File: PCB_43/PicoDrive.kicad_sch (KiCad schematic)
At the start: 28 parts, among them J1 Conn_02x08_Row_Letter_Last, J3 OLED SCREEN CONN, J4 Micro_SD_Card_Det1, Q3 2N2219, U1 Pico, U2 TSR_1-2450

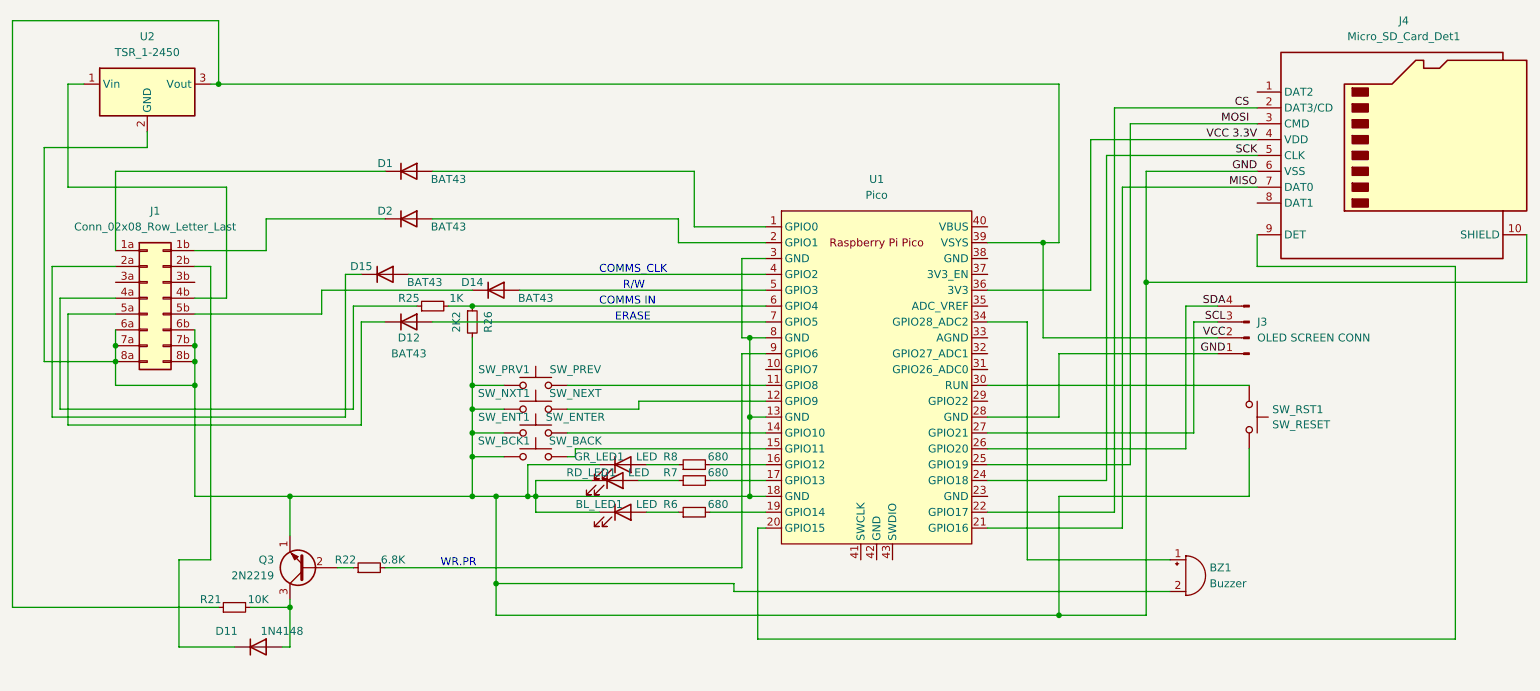
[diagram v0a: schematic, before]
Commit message: Added to PCB a connector for MDV_Control boards
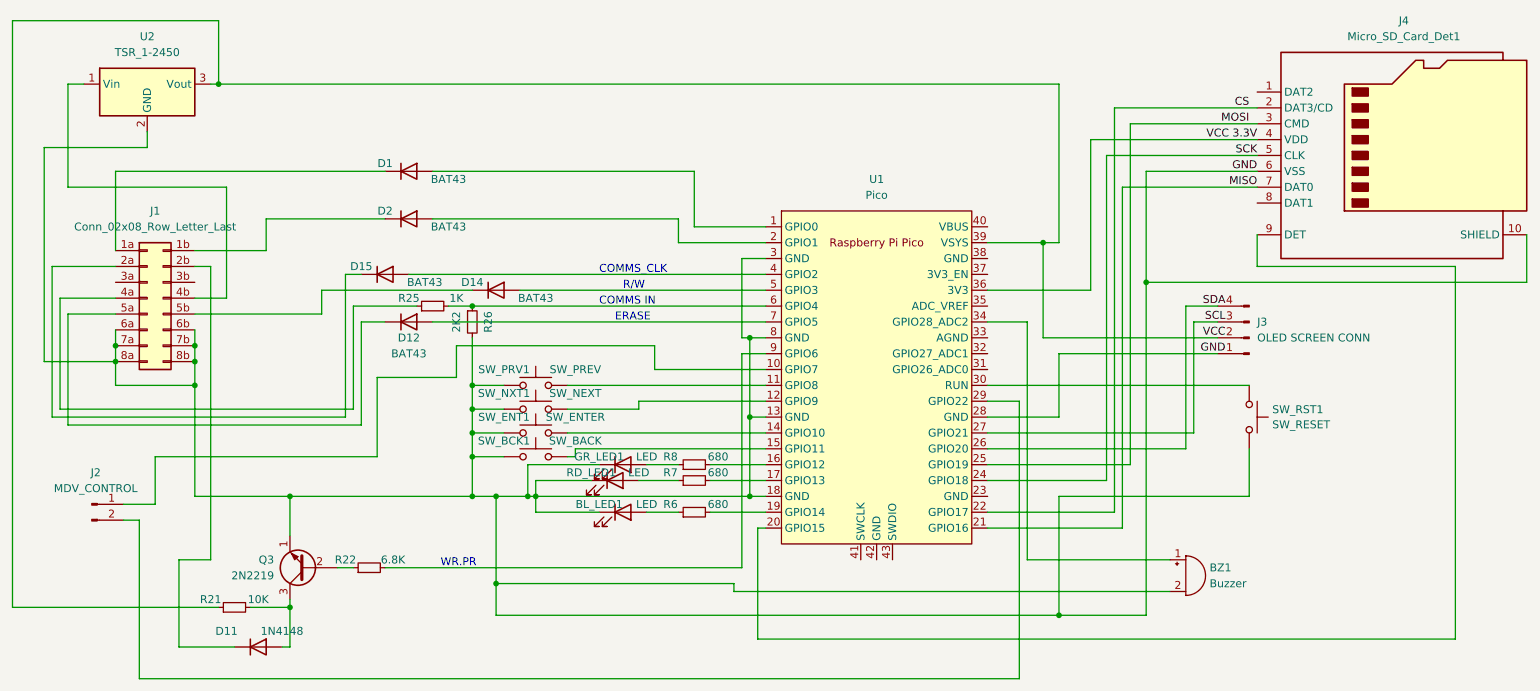
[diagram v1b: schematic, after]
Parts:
- added J2: MDV_CONTROL, Connector_PinHeader_2.54mm:PinHeader_1x02_P2.54mm_Vertical, symbol Connector:Conn_01x02_Pin
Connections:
- net at U1.10 (GPIO7): now also J2.1 (Pin_1)
- net at U1.29 (GPIO22): now also J2.2 (Pin_2)
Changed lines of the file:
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@@
+    (stroke (width 0) (type default))
+  )
+  (wire (pts (xy 88.9 91.44) (xy 53.34 91.44))
     (stroke (width 0) (type default))
   )
@@
     (stroke (width 0) (type default))
   )
+  (wire (pts (xy 53.34 91.44) (xy 53.34 99.06))
+    (stroke (width 0) (type default))
+  )
   (wire (pts (xy 146.05 113.03) (xy 215.9 113.03))
     (stroke (width 0) (type default))
@@
     (stroke (width 0) (type default))
   )
+  (wire (pts (xy 88.9 78.74) (xy 88.9 91.44))
+    (stroke (width 0) (type default))
+  )
   (wire (pts (xy 186.69 95.25) (xy 205.74 95.25))
     (stroke (width 0) (type default))
@@
     (stroke (width 0) (type default))
   )
+  (wire (pts (xy 191.77 127) (xy 50.8 127))
+    (stroke (width 0) (type default))
+  )
   (wire (pts (xy 119.38 91.44) (xy 120.65 91.44))
     (stroke (width 0) (type default))
@@
     (stroke (width 0) (type default))
   )
+  (wire (pts (xy 101.6 78.74) (xy 88.9 78.74))
+    (stroke (width 0) (type default))
+  )
   (wire (pts (xy 142.24 92.71) (xy 151.13 92.71))
     (stroke (width 0) (type default))
@@
     (stroke (width 0) (type default))
   )
+  (wire (pts (xy 50.8 127) (xy 50.8 101.6))
+    (stroke (width 0) (type default))
+  )
   (wire (pts (xy 208.28 48.26) (xy 229.87 48.26))
     (stroke (width 0) (type default))
@@
     (stroke (width 0) (type default))
   )
+  (wire (pts (xy 151.13 77.47) (xy 133.35 77.47))
+    (stroke (width 0) (type default))
+  )
   (wire (pts (xy 229.87 60.96) (xy 229.87 55.88))
     (stroke (width 0) (type default))
@@
     (stroke (width 0) (type default))
   )
+  (wire (pts (xy 133.35 77.47) (xy 133.35 73.66))
+    (stroke (width 0) (type default))
+  )
   (wire (pts (xy 64.77 48.26) (xy 39.37 48.26))
     (stroke (width 0) (type default))
@@
     (stroke (width 0) (type default))
   )
+  (wire (pts (xy 133.35 73.66) (xy 101.6 73.66))
+    (stroke (width 0) (type default))
+  )
   (wire (pts (xy 186.69 100.33) (xy 207.01 100.33))
     (stroke (width 0) (type default))
@@
     (stroke (width 0) (type default))
   )
+  (wire (pts (xy 53.34 99.06) (xy 48.26 99.06))
+    (stroke (width 0) (type default))
+  )
   (wire (pts (xy 186.69 90.17) (xy 218.44 90.17))
     (stroke (width 0) (type default))
   )
+  (wire (pts (xy 48.26 101.6) (xy 50.8 101.6))
+    (stroke (width 0) (type default))
+  )
   (wire (pts (xy 109.22 80.01) (xy 104.14 80.01))
     (stroke (width 0) (type default))
@@
     (stroke (width 0) (type default))
   )
+  (wire (pts (xy 191.77 82.55) (xy 191.77 127))
+    (stroke (width 0) (type default))
+  )
   (wire (pts (xy 205.74 43.18) (xy 229.87 43.18))
     (stroke (width 0) (type default))
@@
     (stroke (width 0) (type default))
   )
+  (wire (pts (xy 101.6 73.66) (xy 101.6 78.74))
+    (stroke (width 0) (type default))
+  )
   (wire (pts (xy 212.09 45.72) (xy 229.87 45.72))
     (stroke (width 0) (type default))
@@
   )
   (wire (pts (xy 100.33 67.31) (xy 104.14 67.31))
+    (stroke (width 0) (type default))
+  )
+  (wire (pts (xy 186.69 82.55) (xy 191.77 82.55))
     (stroke (width 0) (type default))
   )
@@
         )
       )
+    )
+  )
+  (symbol (lib_id "Connector:Conn_01x02_Pin") (at 43.18 99.06 0) (unit 1)
+    (in_bom yes) (on_board yes) (dnp no) (fields_autoplaced)
+    (property "Reference" "J2" (at 43.815 93.98 0)
+      (effects (font (size 1.27 1.27)))
+    )
+    (property "Value" "MDV_CONTROL" (at 43.815 96.52 0)
+      (effects (font (size 1.27 1.27)))
+    )
+    (property "Footprint" "Connector_PinHeader_2.54mm:PinHeader_1x02_P2.54mm_Vertical" (at 43.18 99.06 0)
+      (effects (font (size 1.27 1.27)) hide)
+    )
+    (property "Datasheet" "~" (at 43.18 99.06 0)
+      (effects (font (size 1.27 1.27)) hide)
+    )
+    (pin "1")
+    (pin "2")
+    (instances
+      (project "PicoDrive"
+        (path "/24be1e86-cc83-4669-8c55-f41abaed0d99"
+          (reference "J2") (unit 1)
+        )
+      )
